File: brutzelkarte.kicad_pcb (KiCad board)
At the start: 2 copper layers, 100 x 71.8 mm, 106 parts, among them CON1 N64-Cartridge, CON2 USB_B_Micro, CON3 Conn_01x04, CON4 Conn_01x06, CON5 Conn_01x12, Q1 BSS138K, U1 FT232RL, U2 LCMXO2-7000Hx-xTG144x, U3 IS62WV12816EBLL, U4 MCP7940N, U5 S25FL256S, U6 S25FL256S, U7 W25Q_SOIC8, U8 TLV1117LV, Y1 32768

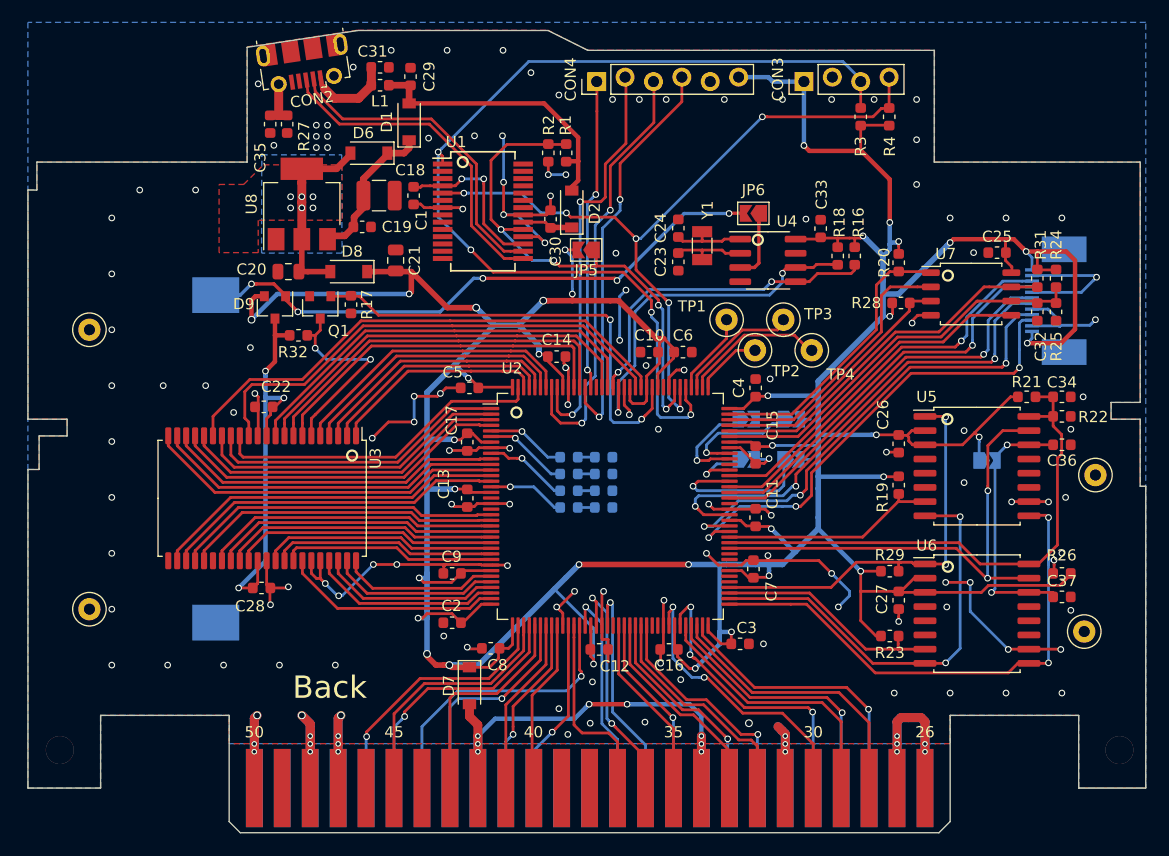
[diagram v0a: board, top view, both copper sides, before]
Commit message: Make a breakout board
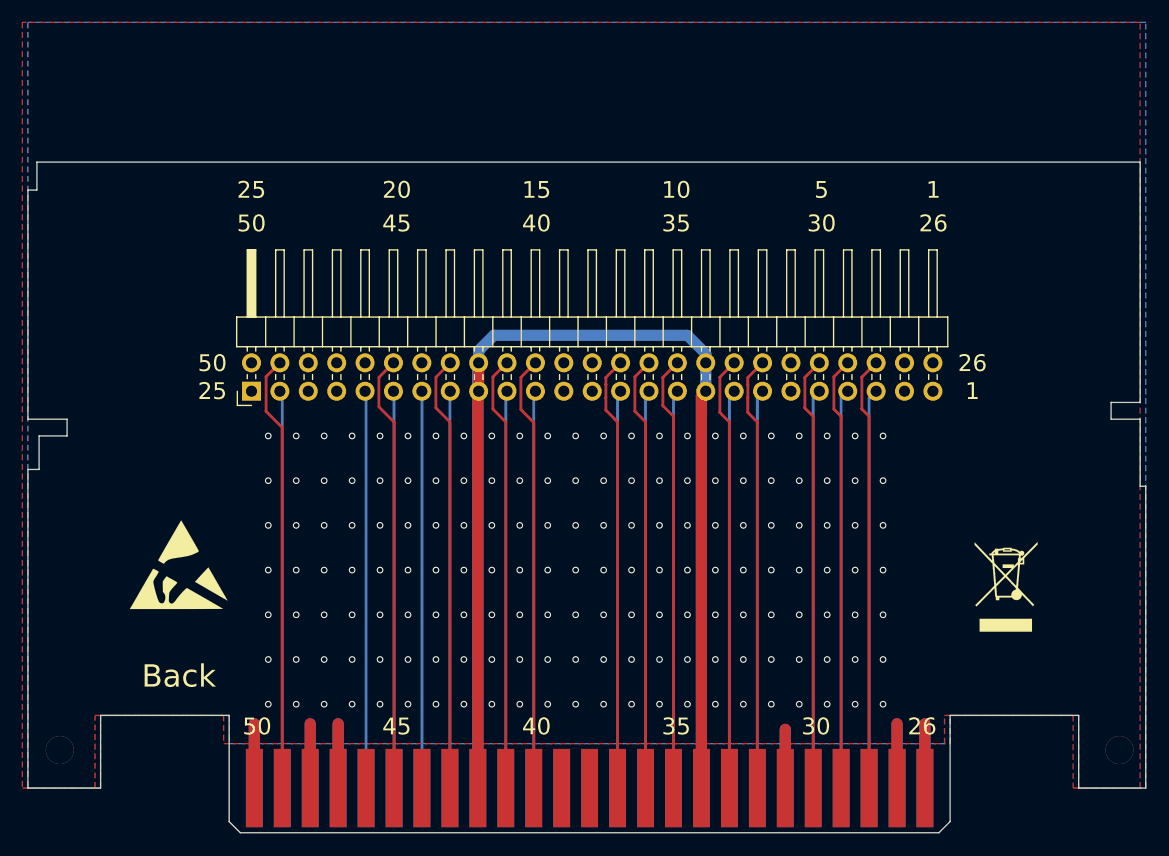
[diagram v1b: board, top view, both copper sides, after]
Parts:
- removed BT1: Battery_Cell, Brutzelkarte:BU2032SM
- removed C1, C10, C11, C12, C13, C14, C15, C16, C17, C19, C2, C22, C25, C26, C27, C28, C3, C30, C33, C36, C37, C4, C5, C6, C7, C8, C9: 100n, Capacitor_SMD:C_0603_1608Metric
- removed C18: 10u, Capacitor_SMD:C_1210_3225Metric
- removed C20: 1u, Capacitor_SMD:C_0805_2012Metric
- removed C21: 47u, Capacitor_SMD:C_0805_2012Metric
- removed C23, C24: 6-9 pF, Capacitor_SMD:C_0603_1608Metric
- removed C29: 4u7, Capacitor_SMD:C_0603_1608Metric
- removed C31, C35: 10n, Capacitor_SMD:C_0603_1608Metric
- removed C32, C34: ?n, Capacitor_SMD:C_0603_1608Metric
- removed CON2: USB_B_Micro, Connector_USB:USB_Micro-B_Molex-105017-0001
- removed CON3: Conn_01x04, Brutzelkarte:PinHeader_1x04_P2.54mm_NoSolder
- removed CON4: Conn_01x06, Brutzelkarte:PinHeader_1x06_P2.54mm_NoSolder
- removed CON5: Conn_01x12, Brutzelkarte:12pinFPC_ConnectorP0.5mm
- removed D1, D2, D6, D7, D8: D_Schottky_Small, Diode_SMD:D_SOD-123
- removed D9: BAT54C, Package_TO_SOT_SMD:SOT-23
- removed G***: LOGO, Brutzelkarte:LOGO_small
- removed GND1, GND2, GND3, GND4, TP1, TP2, TP3, TP4: TestPoint, TestPoint:TestPoint_Loop_D2.50mm_Drill1.0mm
- removed JP1, JP2, JP3, JP4, JP5, JP6, JP7: SolderJumper_2_Open, Jumper:SolderJumper-2_P1.3mm_Open_TrianglePad1.0x1.5mm
- removed L1: Ferrite, Inductor_SMD:L_0603_1608Metric
- removed LD1, LD2, LD3, LD4: LED_Small, LED_SMD:LED_0603_1608Metric
- removed Q1: BSS138K, Package_TO_SOT_SMD:SOT-23
- removed R1: 6k8, Resistor_SMD:R_0603_1608Metric
- removed R12, R13, R14, R15: 330, Resistor_SMD:R_0603_1608Metric
- removed R16, R18: 4k7, Resistor_SMD:R_0603_1608Metric
- removed R17: 2k2, Resistor_SMD:R_0603_1608Metric
- removed R19, R2, R20, R21, R22, R23, R24, R25, R26, R28, R29, R3, R31, R32, R4: 10k, Resistor_SMD:R_0603_1608Metric
- removed R27: 100k, Resistor_SMD:R_0603_1608Metric
- removed U1: FT232RL, Package_SO:SSOP-28_5.3x10.2mm_P0.65mm
- removed U2: LCMXO2-7000Hx-xTG144x, Package_QFP:TQFP-144_20x20mm_P0.5mm
- removed U3: IS62WV12816EBLL, Package_SO:TSOP-II-44_10.16x18.41mm_P0.8mm
- removed U4: MCP7940N, Package_SO:SOIC-8_3.9x4.9mm_P1.27mm
- removed U5, U6: S25FL256S, Package_SO:SOIC-16W_7.5x10.3mm_P1.27mm
- removed U7: W25Q_SOIC8, Package_SO:SOIC-8_5.275x5.275mm_P1.27mm
- removed U8: TLV1117LV, Package_TO_SOT_SMD:SOT-223
- removed Y1: 32768, Crystal:Crystal_SMD_3215-2Pin_3.2x1.5mm
- added J1: Conn_02x25_Odd_Even, Connector_PinHeader_2.54mm:PinHeader_2x25_P2.54mm_Horizontal, F.Cu at (102.5, 90.5)
- added REF**: ESD-Logo_8.9x8mm_SilkScreen, Symbol:ESD-Logo_8.9x8mm_SilkScreen, F.Cu at (96.0, 106.0)
- added REF**: WEEE-Logo_5.6x8mm_SilkScreen, Symbol:WEEE-Logo_5.6x8mm_SilkScreen, F.Cu at (170.0, 108.0)
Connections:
- CON1 pad 13: (no net) -> Net-(CON1-Pad13)
- CON1 pad 14: (no net) -> Net-(CON1-Pad14)
- CON1 pad 24: (no net) -> /fpga/N64_LAUDIO
- CON1 pad 38: (no net) -> Net-(CON1-Pad38)
- CON1 pad 39: (no net) -> Net-(CON1-Pad39)
- CON1 pad 44: (no net) -> Net-(CON1-Pad44)
- CON1 pad 46: (no net) -> Net-(CON1-Pad46)
- CON1 pad 49: (no net) -> /fpga/N64_RAUDIO
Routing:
- net +3V3: track 442.3 -> 0.00 mm, vias 35 -> 0
- net GND: track 271.3 -> 68.0 mm, vias 148 -> 161
- net /fpga/N64_VCC: track 48.2 -> 173.5 mm, vias 8 -> 0
- net /fpga/UART_RX: track 89.7 -> 0.00 mm, vias 4 -> 0
- net /fpga/UART_TX: track 68.0 -> 0.00 mm, vias 6 -> 0
- net /memory/VBAT: track 52.8 -> 0.00 mm, vias 5 -> 0
- net /fpga/ROM_SCK: track 48.6 -> 0.00 mm
- net /fpga/ROM_IO2: track 48.4 -> 0.00 mm, vias 3 -> 0
- net /fpga/RAM_WE: track 46.6 -> 0.00 mm
- net /fpga/USB_DETECT: track 46.0 -> 0.00 mm, vias 4 -> 0
- net /fpga/RAM_DQ4: track 44.2 -> 0.00 mm
- net /fpga/ROM_IO0: track 44.1 -> 0.00 mm, vias 2 -> 0
- net /fpga/EXT3: track 43.9 -> 0.00 mm, vias 3 -> 0
- net /fpga/EXT5: track 42.5 -> 0.00 mm, vias 3 -> 0
- net /fpga/EXT4: track 42.2 -> 0.00 mm, vias 3 -> 0
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- removed copper zone on B.Cu, net /power/+3V3_REG
- removed copper zone on F.Cu, net /power/+3V3_REG
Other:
- board size 100 x 71.8 mm -> 100 x 60 mm
- net class Default: clearance 0.2 -> 0.25
- rule trace_clearance: 0.2 -> 0.25
- board text removed: "+3.3V"
- board text removed: "2020"
- board text removed: "Brutzelkarte"
- board text removed: "Devkit 1.1"
- board text removed: "GND"
- board text removed: "RX"
- board text removed: "TCK"
- board text removed: "TDI"
- board text removed: "TDO"
- board text removed: "TMS"
- board text removed: "TX"
- board text removed: "VIO"
- board text removed: "ca 1,2mm dick"

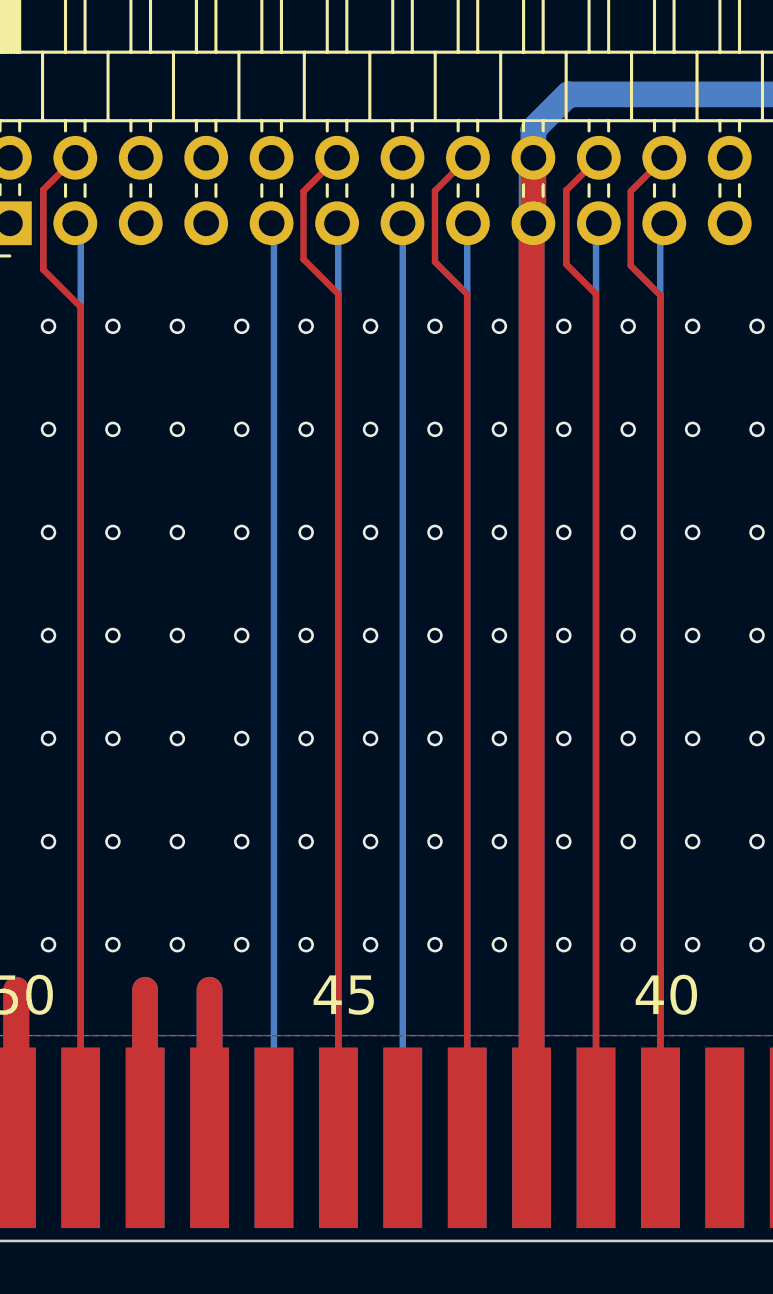
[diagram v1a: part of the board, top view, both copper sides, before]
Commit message: Add pin 44 and update to KiCad 6.0
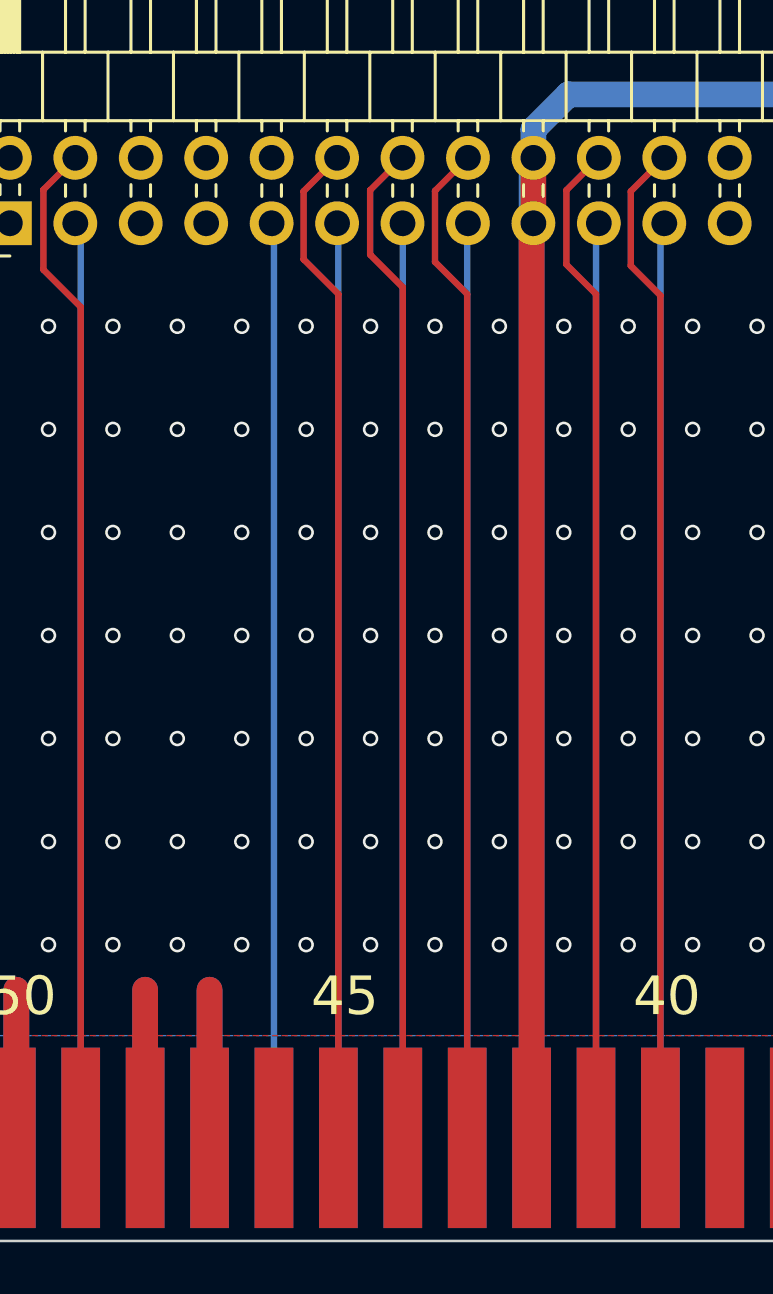
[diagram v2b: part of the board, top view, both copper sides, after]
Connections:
- CON1 pad 13: Net-(CON1-Pad13) -> unconnected-(CON1-Pad13)
- CON1 pad 14: Net-(CON1-Pad14) -> unconnected-(CON1-Pad14)
- CON1 pad 38: Net-(CON1-Pad38) -> unconnected-(CON1-Pad38)
- CON1 pad 39: Net-(CON1-Pad39) -> unconnected-(CON1-Pad39)
- CON1 pad 44: Net-(CON1-Pad44) -> /fpga/N64_INT
- CON1 pad 46: Net-(CON1-Pad46) -> unconnected-(CON1-Pad46)
- J1 pad 10: Net-(J1-Pad10) -> unconnected-(J1-Pad10)
- J1 pad 14: Net-(J1-Pad14) -> /fpga/N64_INT
- J1 pad 23: Net-(J1-Pad23) -> unconnected-(J1-Pad23)
- J1 pad 24: Net-(J1-Pad24) -> unconnected-(J1-Pad24)
- J1 pad 25: Net-(J1-Pad25) -> unconnected-(J1-Pad25)
- J1 pad 26: Net-(J1-Pad26) -> unconnected-(J1-Pad26)
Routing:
- net /fpga/N64_INT: track 0.00 -> 39.1 mm
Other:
- net class Default removed
- net class differential routing removed
